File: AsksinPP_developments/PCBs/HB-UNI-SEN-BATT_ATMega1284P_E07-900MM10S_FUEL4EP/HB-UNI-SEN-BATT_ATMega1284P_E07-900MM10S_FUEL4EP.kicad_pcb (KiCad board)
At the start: 2 copper layers, 75 x 75 mm, 59 parts, among them J1 Conn_01x02, J10 charge, J11 ePaper connector, J12 FTDI Debuger, J13 U.FL connector, J2 Conn_01x02, J3 Conn_01x02, J4 Conn_01x02, J5 ISP Programmer, J6 Conn_01x04, J7 Conn_01x04, J8 Conn_01x04, J9 Conn_01x04, Q1 IRLU024N, SW1 Config button, SW2 Reset button, U1 ATmega1284P-AU, U2 TPS61221DCK, Y1 8MHz

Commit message: PCBs: HB_TH_Sensor_SHT45_AllInOne_FUEL4EP and HB-UNI-SEN-BATT_ATMega1284P_E07-900MM10S_FUEL4EP: fix of wrong LCSC part numbers
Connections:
- R8 pad 1: /plusBAT -> unconnected-(R8-Pad1)
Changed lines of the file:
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@@
   (net 57 "unconnected-(Module1-Pad5B)")
   (net 58 "unconnected-(Module1-Pad5C)")
+  (net 59 "unconnected-(R8-Pad1)")
   (footprint "LED_SMD:LED_0805_2012Metric_Pad1.15x1.40mm_HandSolder" (layer "F.Cu")
     (at 9.1635 -72.7995)
@@
     (descr "Capacitor SMD 0402 (1005 Metric), square (rectangular) end terminal, IPC_7351 nominal, (Body size source: IPC-SM-782 page 76, https://www.pcb-3d.com/wordpress/wp-content/uploads/ipc-sm-782a_amendment_1_and_2.pdf), generated with kicad-footprint-generator")
     (tags "capacitor")
-    (property "LCSC" "C7171")
-    (property "Sheetfile" "HB-UNI-SEN-BATT_ATMega1284P_E07-900MM10S_FUEL4EP.kicad_sch")
-    (property "Sheetname" "")
-    (property "TYPE" "CASE-A_3216")
+    (property "LCSC" "C15525")
+    (property "Sheetfile" "HB-UNI-SEN-BATT_ATMega1284P_E07-900MM10S_FUEL4EP.kicad_sch")
+    (property "Sheetname" "")
+    (property "TYPE" "0402")
     (attr smd)
     (fp_text reference "C1" (at -1.905 0) (layer "F.SilkS")
@@
     (fp_line (start 1 -0.625) (end 1 0.625) (layer "F.Fab") (width 0.1))
     (pad "1" smd roundrect (at -1 0 180) (size 1.2 1.4) (layers "F.Cu" "F.Paste" "F.Mask") (roundrect_rratio 0.2083333333)
-      (net 18 "/plusBAT") (pintype "passive"))
+      (net 59 "unconnected-(R8-Pad1)") (pintype "passive"))
     (pad "2" smd roundrect (at 1 0 180) (size 1.2 1.4) (layers "F.Cu" "F.Paste" "F.Mask") (roundrect_rratio 0.2083333333)
       (net 7 "/A0") (pintype "passive"))

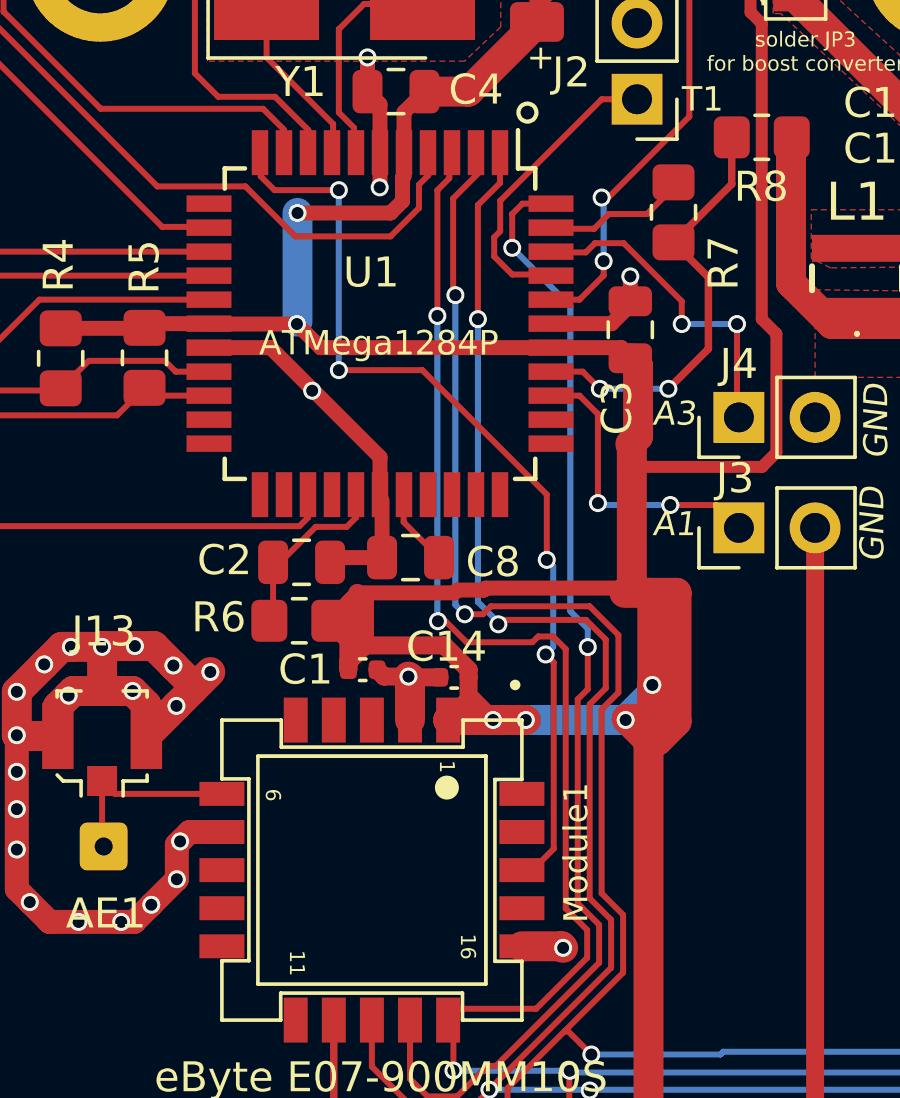
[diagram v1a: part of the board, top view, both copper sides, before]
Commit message: PCBs: documentation updates / PCBs: HB-UNI-SEN-BATT_ATMega1284P_E07-868MS10_FUEL4EP, HB-UNI-SEN-BATT_ATMega1284P_E07-868MS10_FRAM_FUEL4EP, HB-UNI-SEN-BATT_ATMega1284P_E07-900MM10S_FUEL4EP: fix of wrong LCSC number for R7
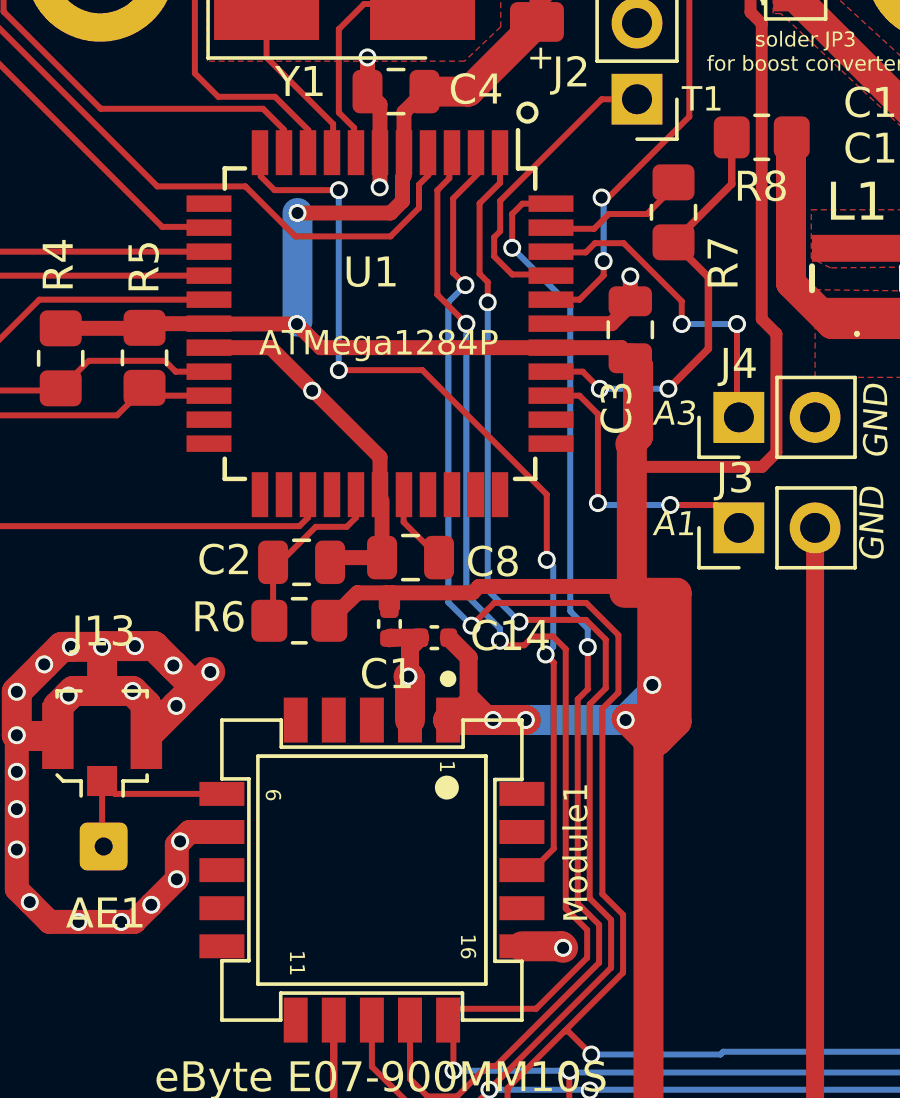
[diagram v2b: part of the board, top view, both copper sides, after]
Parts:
- moved C1 1.76 mm to (33.1, -40.9), turned to -90 degrees
- moved C14 1.48 mm to (34.6, -40.4)
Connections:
- R8 pad 1: unconnected-(R8-Pad1) -> /plusBAT
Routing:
- net VCC: track 246.4 -> 235.0 mm
- net /MISO: track 91.6 -> 92.5 mm
- net /SCK: track 86.0 -> 85.2 mm
- net /MOSI: track 89.3 -> 88.7 mm
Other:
- board text added: "Version 1.1 - 02/2024 (KiCAD 6)"
- board text removed: "Version 1.0 - 09/2023 (KiCAD 6)"

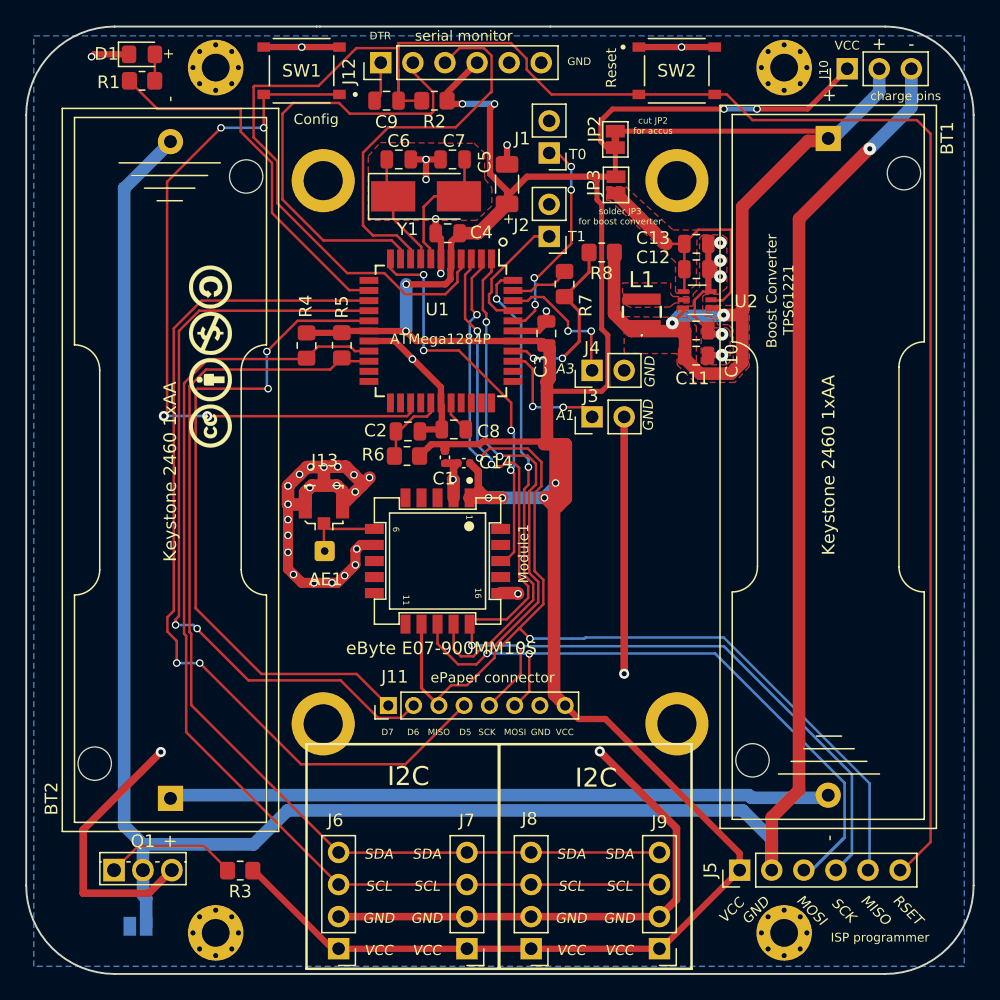
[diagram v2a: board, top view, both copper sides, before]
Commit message: PCBs/HB-UNI-SEN-BATT_ATMega1284P_E07-900MM10S_FUEL4EP: migration to KiCAD 8, LCSC fixes; PCBs/HB-UNI-SEN-BATT_ATMega1284P_E07-868MS10_FUEL4EP: BOM update
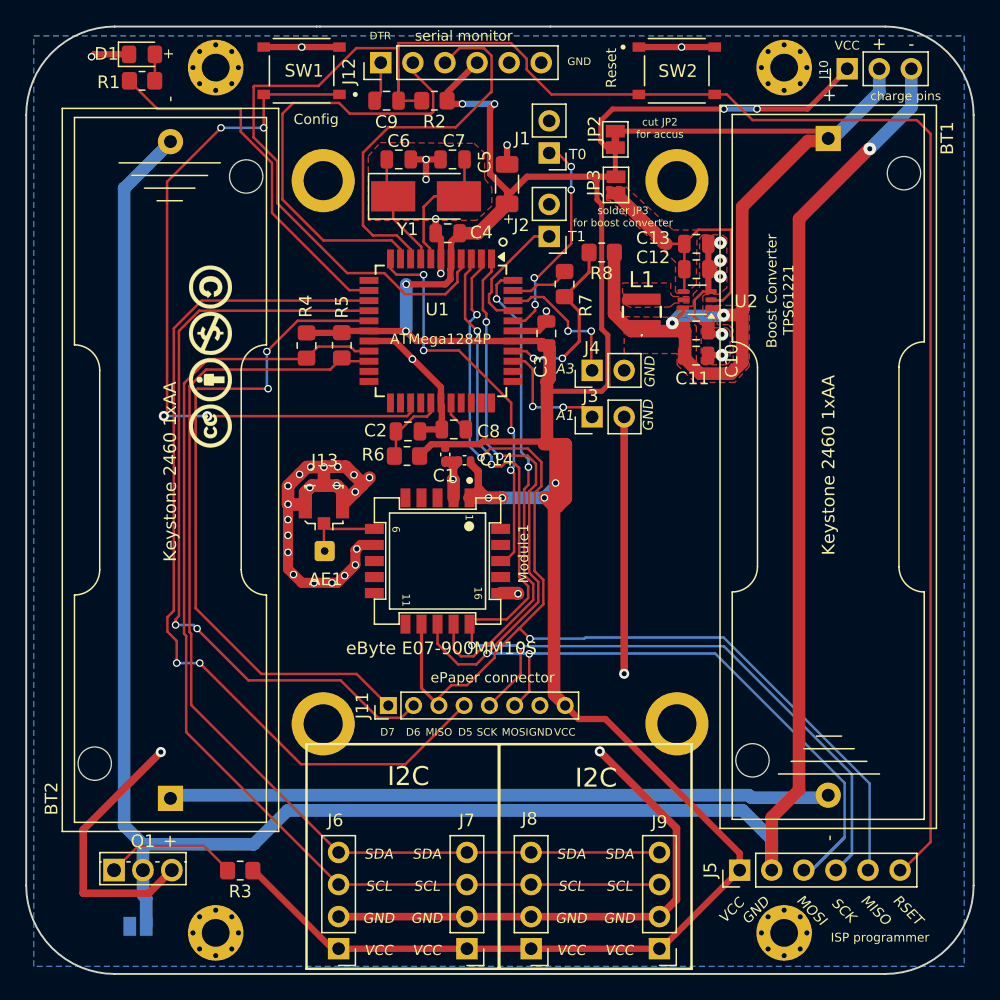
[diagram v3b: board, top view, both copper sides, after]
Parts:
- moved C14 0.23 mm to (34.7, -40.7)
- moved C1 0.23 mm to (33.2, -41.1)
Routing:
- net GND: track 176.8 -> 178.0 mm
- net VCC: track 235.0 -> 234.4 mm
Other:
- board text added: "Version 1.2 - 09/2024 (KiCAD 8)"
- board text removed: "Version 1.1 - 02/2024 (KiCAD 6)"

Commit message: added PCBs/I2C_Module_BME680_small_FUEL4EP; corrected JLCPCB miinimum spacing in DRC rules
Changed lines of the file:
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@@
 		)
 		(fp_text user "11"
-			(at 8.1 7.5 270)
+			(at 8.1 7.5 -90)
 			(unlocked yes)
 			(layer "F.SilkS")
@@
 		)
 		(fp_text user "1"
-			(at 1.55 2.5 270)
+			(at 1.55 2.5 -90)
 			(unlocked yes)
 			(layer "F.SilkS")
@@
 		)
 		(fp_text user "6"
-			(at 2.5 8.3 270)
+			(at 2.5 8.3 -90)
 			(unlocked yes)
 			(layer "F.SilkS")
@@
 		)
 		(fp_text user "16"
-			(at 7.55 1.8 270)
+			(at 7.55 1.8 -90)
 			(unlocked yes)
 			(layer "F.SilkS")

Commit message: PCB updates
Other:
- board text added: "JLCJLCJLCJLC"
